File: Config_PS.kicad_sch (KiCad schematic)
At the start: 13 parts, among them J1 Barrel_Jack_Switch, J2 Conn_01x03_Pin, J3 Screw_Terminal_01x02, U1 LM317_TO-220, U2 LM7805_TO220

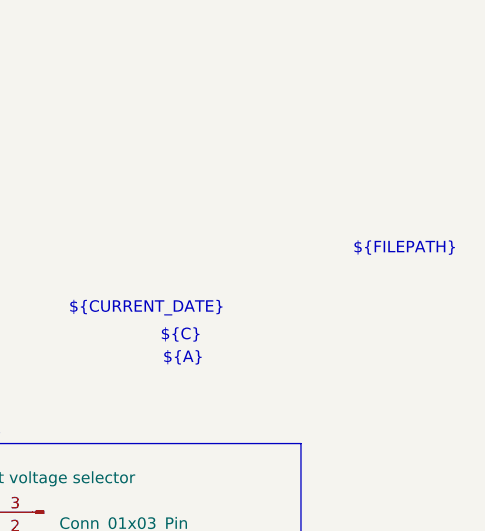
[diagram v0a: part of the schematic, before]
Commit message: deleted date in the schematic design
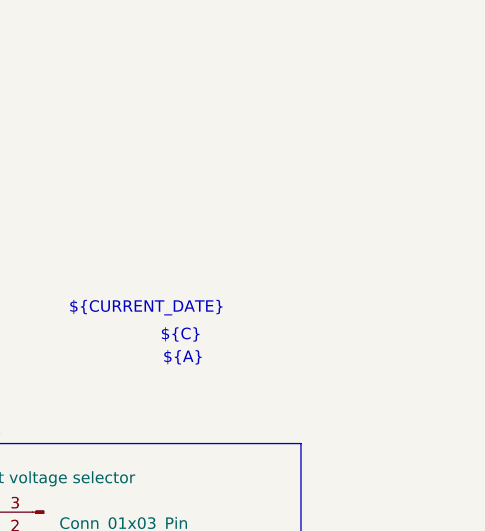
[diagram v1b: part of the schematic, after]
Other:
- note removed: "${FILEPATH}"
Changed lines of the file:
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@@
-		)
-	)
-	(text "${FILEPATH}"
-		(exclude_from_sim no)
-		(at 234.442 71.12 0)
-		(effects
-			(font
-				(size 1.27 1.27)
-			)
 		)
 	)

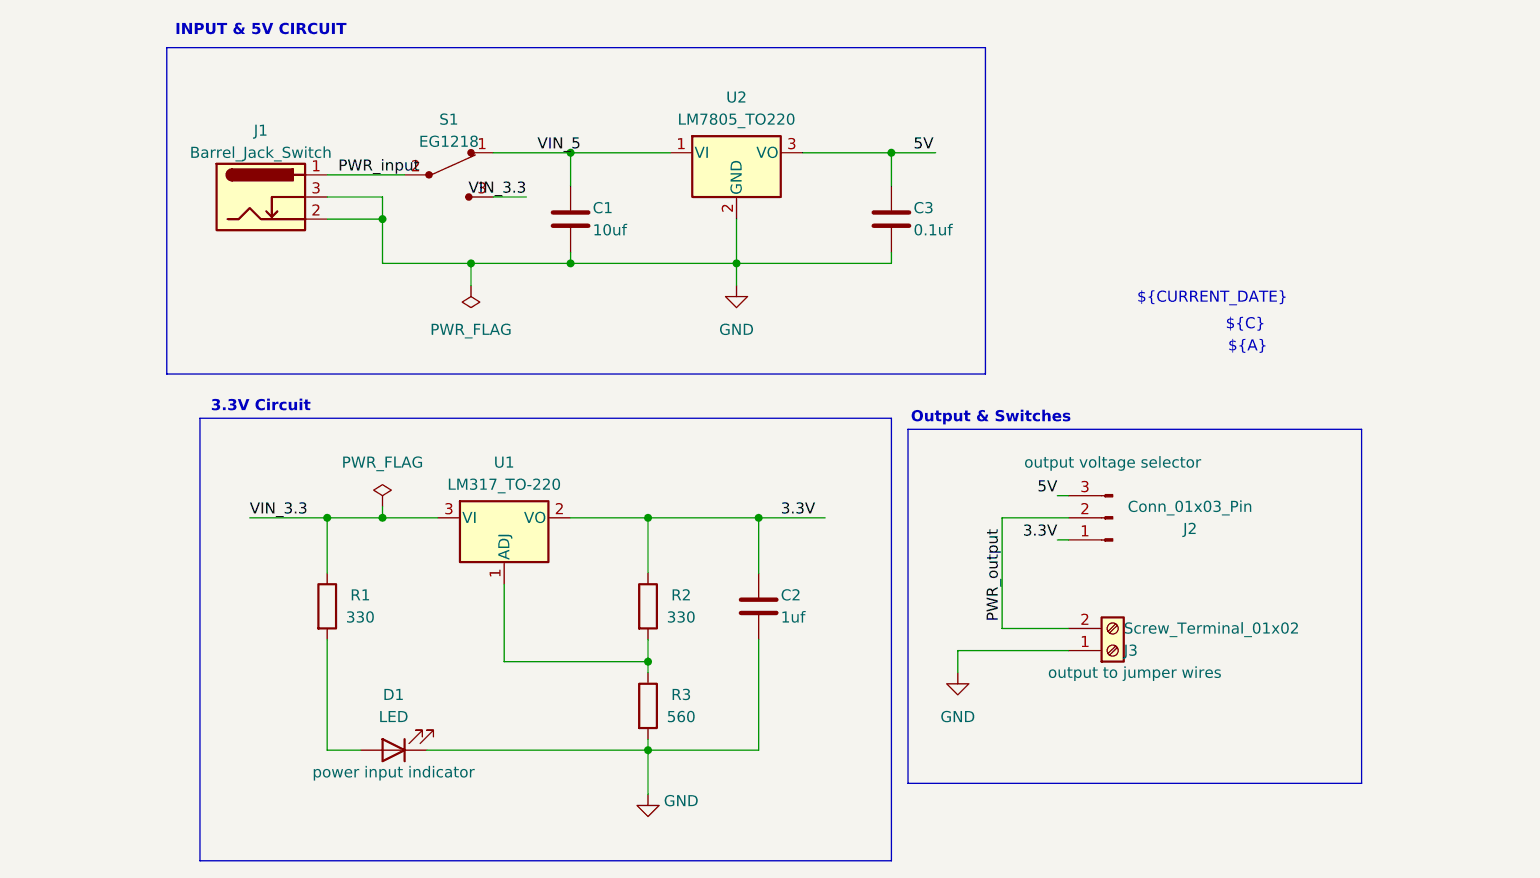
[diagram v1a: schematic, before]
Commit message: added custom logo
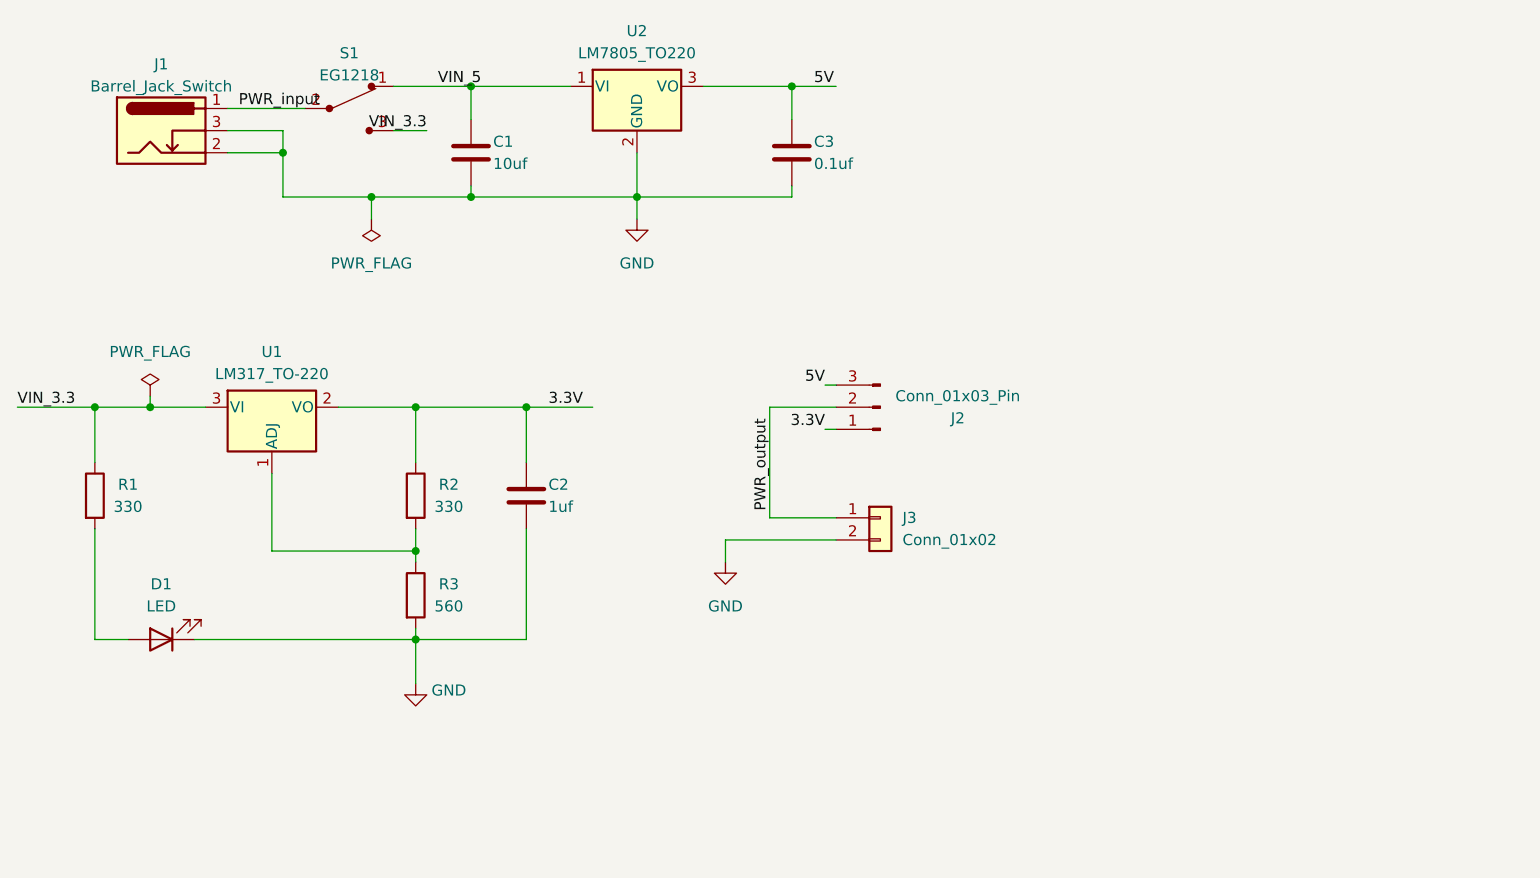
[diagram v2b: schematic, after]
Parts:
- removed J3: Screw_Terminal_01x02, TerminalBlock_Phoenix:TerminalBlock_Phoenix_MKDS-1,5-2_1x02_P5.00mm_Horizontal, symbol Connector:Screw_Terminal_01x02
- added J3: Conn_01x02, symbol Connector_Generic:Conn_01x02
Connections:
- net GND: now also J3.2 (Pin_2)
- net PWR_output: now also J3.1 (Pin_1)
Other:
- note removed: "${A}"
- note removed: "${CURRENT_DATE}"
- note removed: "${C}"
- note removed: "3.3V Circuit"
- note removed: "INPUT & 5V CIRCUIT"
- note removed: "Output & Switches"
- moved on the sheet: C1, C2, C3, D1, J1, J2, R1, R2, R3, S1, U1, U2
